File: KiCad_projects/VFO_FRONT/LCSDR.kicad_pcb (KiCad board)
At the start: 2 copper layers, 71 x 82 mm, 36 parts, among them J1 RX/TX, J10 MANAGEMENT, J12 Conn_01x01, J13 Conn_01x01, J14 Conn_01x01, J15 Conn_01x01, SW1 RESET, SW2 RX/TX, SW3 BEND-, SW4 BEND+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

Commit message: Fix some small issues and first tantal release
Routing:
- net /KEYBOARD: track 41.9 -> 109.8 mm, vias 0 -> 1
- net GND: track 1.70 -> 12.9 mm, vias 0 -> 2
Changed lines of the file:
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@@
   (general
     (links 83)
-    (no_connects 1)
-    (area 70.949999 38.949999 142.050001 121.050001)
+    (no_connects 0)
+    (area 70.252381 38.225 142.74762 121.875)
     (thickness 1.6)
     (drawings 25)
-    (tracks 207)
+    (tracks 223)
     (zones 0)
     (modules 36)
@@
   )
   (layers
-    (0 F.Cu signal hide)
-    (31 B.Cu signal hide)
+    (0 F.Cu signal)
+    (31 B.Cu signal)
     (32 B.Adhes user)
     (33 F.Adhes user)
@@
     (visible_elements 7FFFFF7F)
     (pcbplotparams
-      (layerselection 0x010d0_80000001)
+      (layerselection 0x010f0_80000001)
       (usegerberextensions true)
       (excludeedgelayer true)
@@
     (effects (font (size 1.5 1.5) (thickness 0.3)))
   )
+  (segment (start 112.8 44.95) (end 109.05 44.95) (width 0.4) (layer F.Cu) (net 1))
+  (via (at 108 52) (size 0.6) (drill 0.4) (layers F.Cu B.Cu) (net 1))
+  (segment (start 108 46.5) (end 108 52) (width 0.4) (layer B.Cu) (net 1))
+  (via (at 108 46.5) (size 0.6) (drill 0.4) (layers F.Cu B.Cu) (net 1))
+  (segment (start 108 46) (end 108 46.5) (width 0.4) (layer F.Cu) (net 1))
+  (segment (start 109.05 44.95) (end 108 46) (width 0.4) (layer F.Cu) (net 1))
   (segment (start 86.9 73.2) (end 88.55 73.2) (width 0.4) (layer B.Cu) (net 1))
   (segment (start 127 107.3) (end 127.05 107.3) (width 0.4) (layer B.Cu) (net 1))
@@
   (segment (start 81.66 111.34) (end 81.5 111.34) (width 0.4) (layer B.Cu) (net 9))
   (segment (start 81.5 111.34) (end 81.64 111.34) (width 0.4) (layer B.Cu) (net 9))
+  (segment (start 81.5 91.02) (end 80.02 91.02) (width 0.4) (layer B.Cu) (net 10))
+  (segment (start 115 80.5) (end 119.7 80.5) (width 0.4) (layer F.Cu) (net 10))
+  (via (at 115 80.5) (size 0.6) (drill 0.4) (layers F.Cu B.Cu) (net 10))
+  (segment (start 104 80.5) (end 115 80.5) (width 0.4) (layer B.Cu) (net 10))
+  (segment (start 93 69.5) (end 104 80.5) (width 0.4) (layer B.Cu) (net 10))
+  (segment (start 81 69.5) (end 93 69.5) (width 0.4) (layer B.Cu) (net 10))
+  (segment (start 78.5 72) (end 81 69.5) (width 0.4) (layer B.Cu) (net 10))
+  (segment (start 78.5 89.5) (end 78.5 72) (width 0.4) (layer B.Cu) (net 10))
+  (segment (start 80.02 91.02) (end 78.5 89.5) (width 0.4) (layer B.Cu) (net 10))
   (segment (start 121.8 71.2) (end 119.7 73.3) (width 0.4) (layer F.Cu) (net 10))
-  (segment (start 119.7 73.3) (end 119.7 95.5) (width 0.4) (layer F.Cu) (net 10))
+  (segment (start 119.7 73.3) (end 119.7 80.5) (width 0.4) (layer F.Cu) (net 10))
+  (segment (start 119.7 80.5) (end 119.7 95.5) (width 0.4) (layer F.Cu) (net 10))
   (segment (start 131.6 71.2) (end 121.8 71.2) (width 0.4) (layer F.Cu) (net 10))
   (segment (start 121.8 71.2) (end 121.8 68.5) (width 0.4) (layer F.Cu) (net 10))

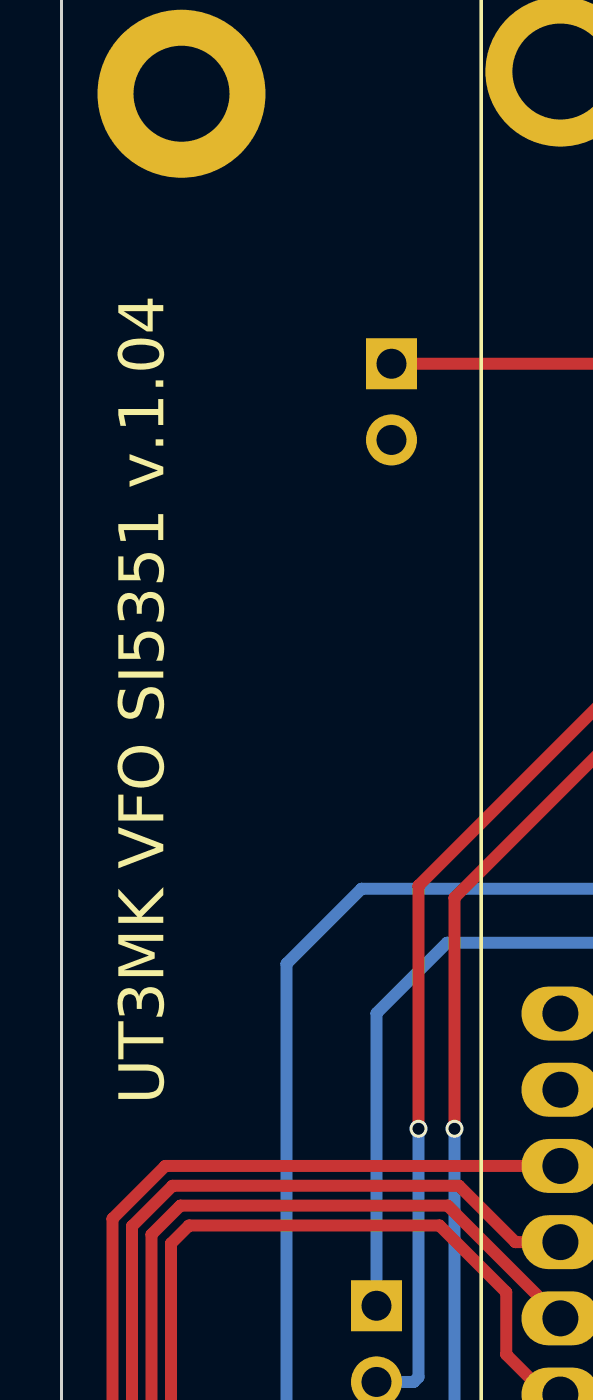
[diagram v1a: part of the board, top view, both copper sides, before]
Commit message: Fix Issues with PCB Silk Text
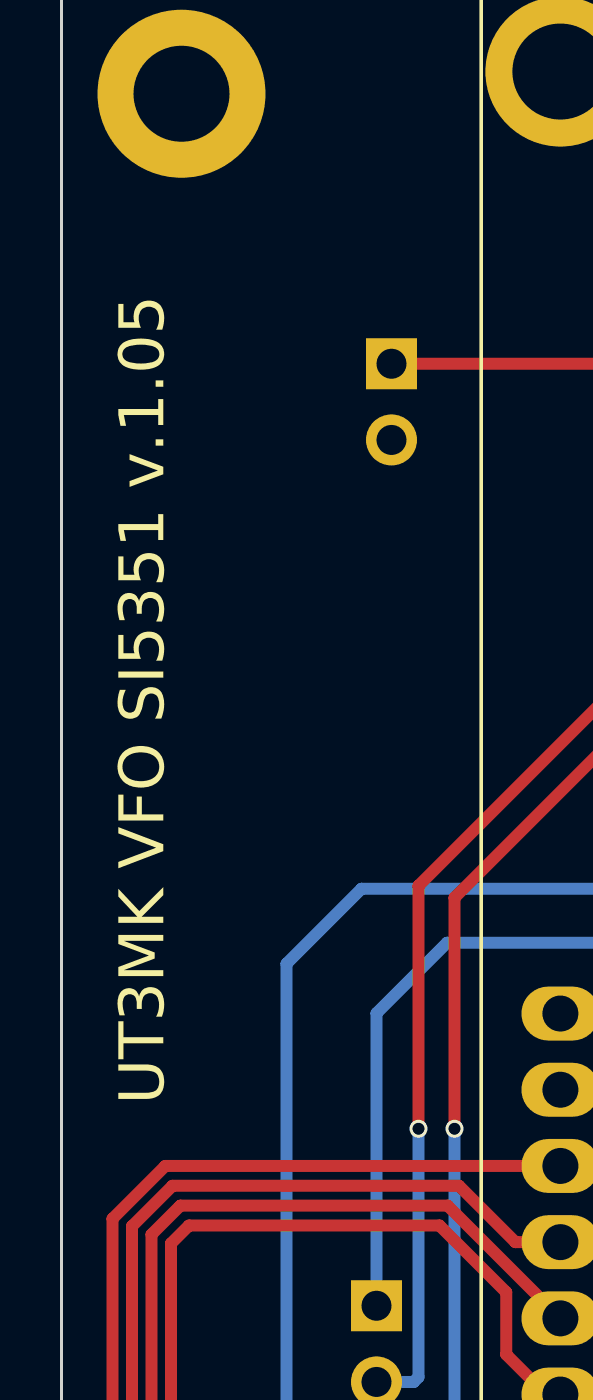
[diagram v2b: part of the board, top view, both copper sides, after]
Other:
- board text added: "UT3MK VFO SI5351 v.1.05"
- board text removed: "UT3MK VFO SI5351 v.1.04"
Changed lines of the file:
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@@
     (effects (font (size 1.5 1.5) (thickness 0.3)))
   )
-  (gr_text "UT3MK VFO SI5351 v.1.04" (at 73.7 63.2 90) (layer F.SilkS)
+  (gr_text "UT3MK VFO SI5351 v.1.05" (at 73.7 63.2 90) (layer F.SilkS)
     (effects (font (size 1.5 1.5) (thickness 0.3)))
   )
